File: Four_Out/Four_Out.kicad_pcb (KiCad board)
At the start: 2 copper layers, 60.7 x 66.3 mm, 23 parts, among them J1 String1, J2 String2, J3 String3, J4 String4, J5 Power In, J6 Expansion Header, U1 74LS125

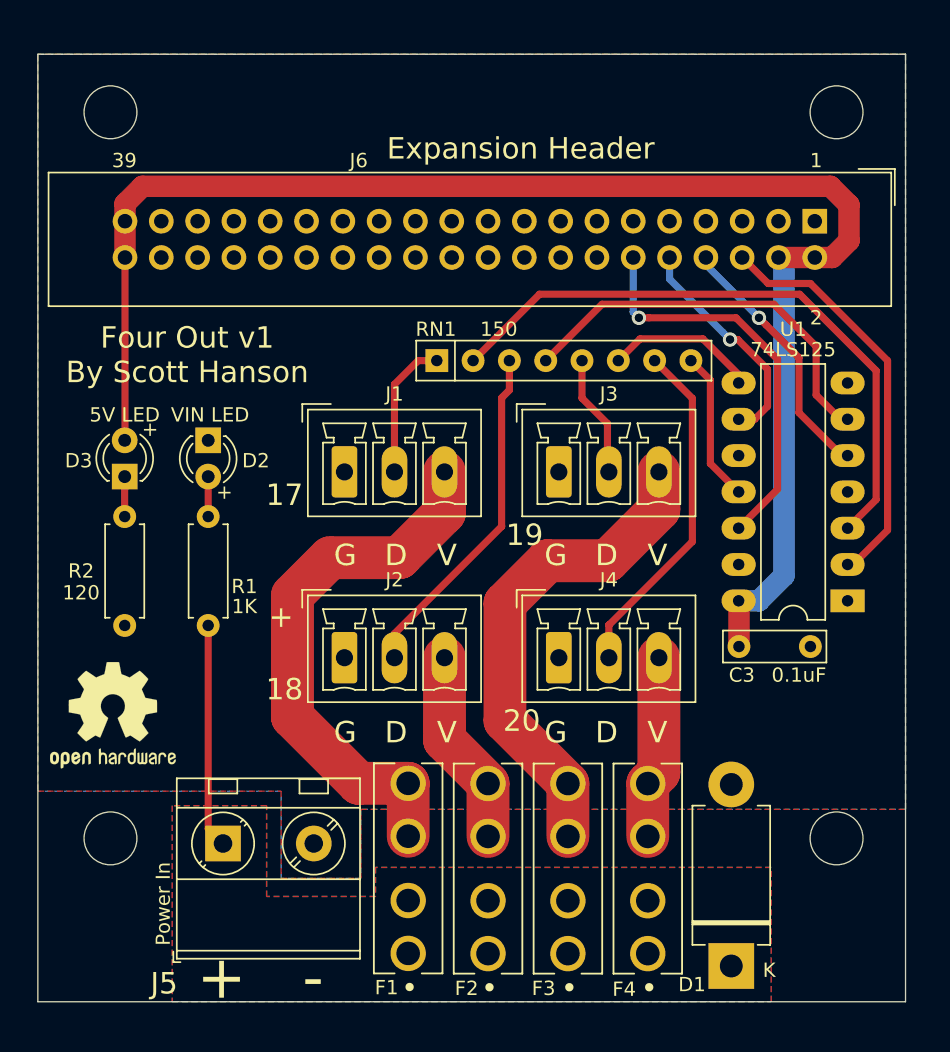
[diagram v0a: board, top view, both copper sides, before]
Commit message: fixed BOM, minor tweaks to ground plane and silkscreen
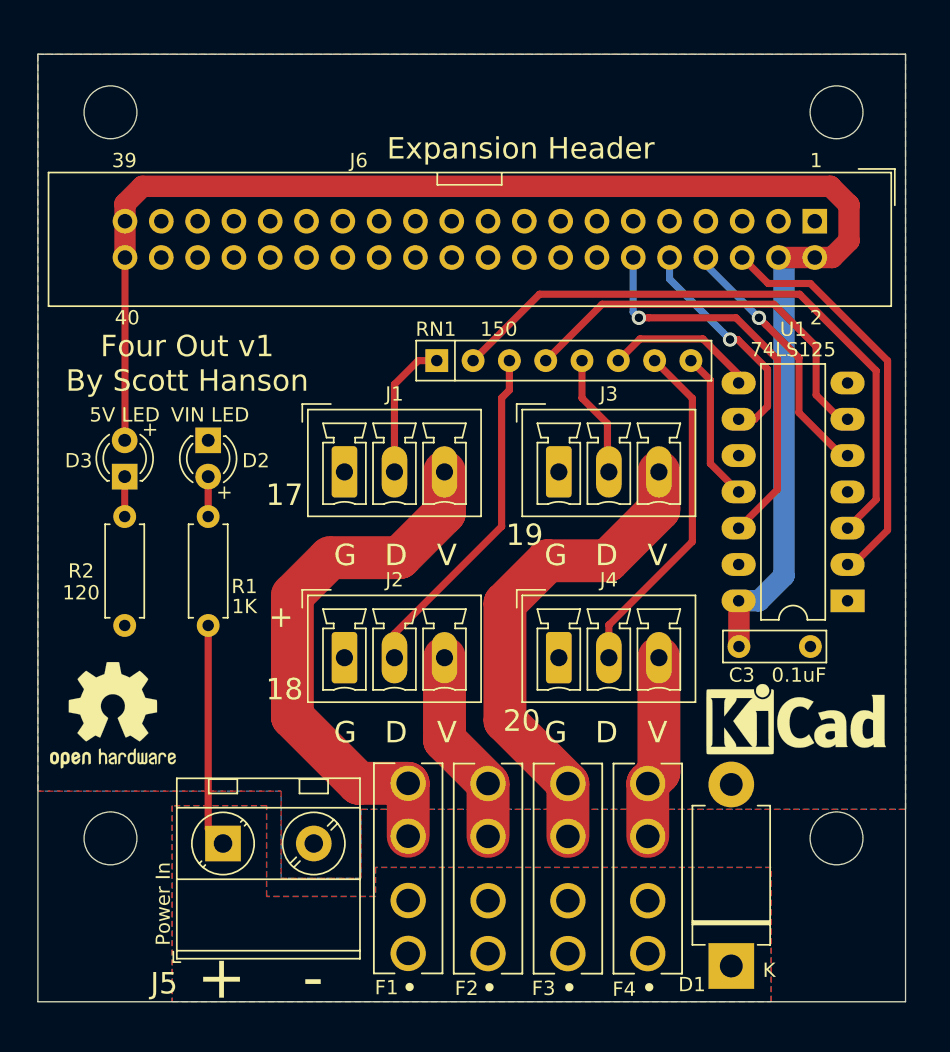
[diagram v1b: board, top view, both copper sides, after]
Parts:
- added REF**: KiCad-Logo_5mm_SilkScreen, Symbol:KiCad-Logo_5mm_SilkScreen, F.Cu at (120.7, 134.4)
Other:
- board text added: "40"

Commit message: rotated header and alt added screw header
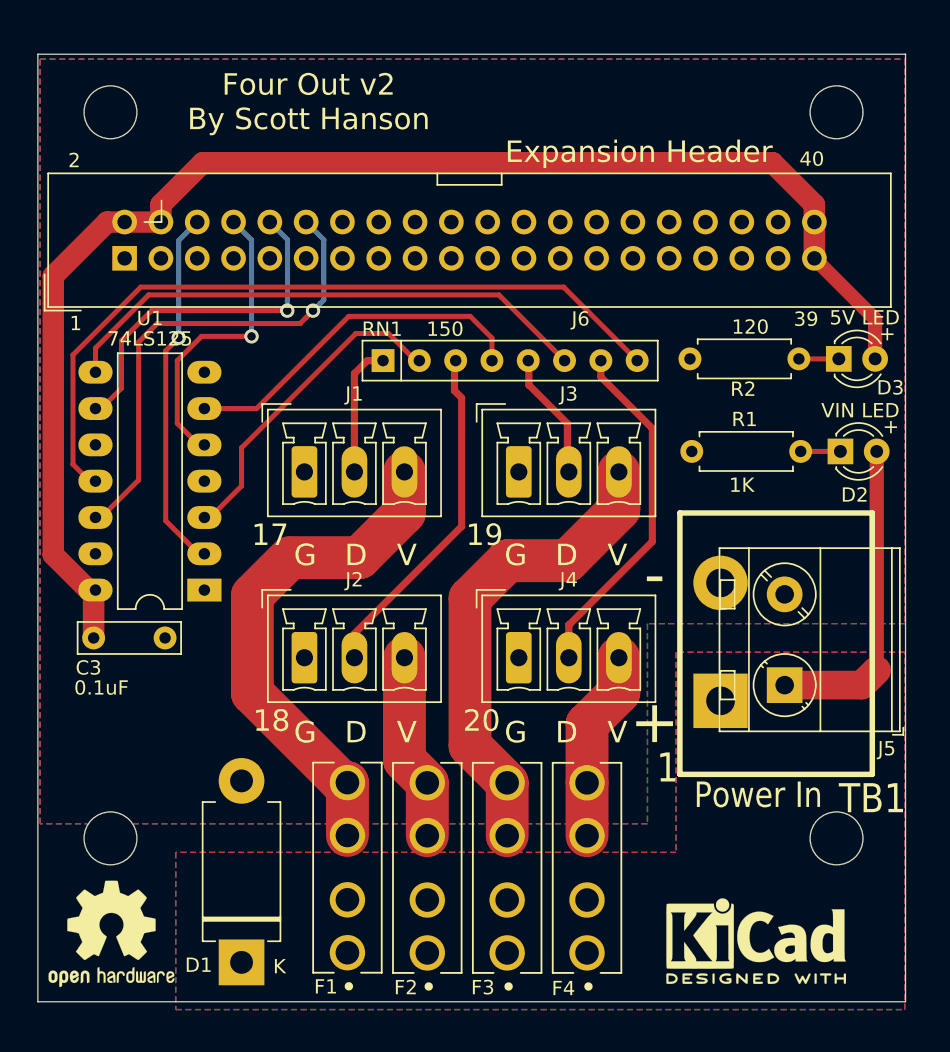
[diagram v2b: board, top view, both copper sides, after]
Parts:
- removed the REF** at (120.7, 134.4)
- added REF**: KiCad-Logo2_5mm_SilkScreen, Symbol:KiCad-Logo2_5mm_SilkScreen, F.Cu at (117.9, 149.4)
- added TB1: Power In, Barrier_Blocks:BARRIER_BLOCK_1ROW_2POS, F.Cu at (119.3, 128.6)
- moved D3 50.6 mm to (123.7, 108.7), turned to 0 degrees
- moved J6 48.4 mm to (73.7, 101.7), turned to 90 degrees
- moved C3 45.2 mm to (71.6, 128.2)
- moved U1 45.0 mm to (79.3, 124.9)
- moved D2 44.2 mm to (123.8, 115.2), turned to 0 degrees
- moved R2 43.7 mm to (113.3, 108.7), turned to 0 degrees
- moved J5 40.8 mm to (119.9, 131.5), turned to 90 degrees
- moved D1 34.3 mm to (81.9, 150.9)
- moved R1 34.1 mm to (113.4, 115.2), turned to 0 degrees
- moved REF** 15.3 mm to (72.8, 148.9)
- moved F1 4.25 mm to (89.3, 144.3)
- moved F2 4.25 mm to (94.9, 144.3)
- moved F3 4.25 mm to (100.5, 144.3)
- moved F4 4.25 mm to (106.1, 144.3)
- moved RN1 3.76 mm to (91.8, 108.8)
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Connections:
- D2 pad 1: GND -> Net-(D2-Pad1)
- D2 pad 2: Net-(D2-Pad2) -> VIN1
- R1 pad 1: Net-(D2-Pad2) -> GND
- R1 pad 2: VIN1 -> Net-(D2-Pad1)
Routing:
- net Net-(RN1-Pad8): track 10.6 -> 53.3 mm
- net Net-(RN1-Pad6): track 10.7 -> 38.0 mm
- net Net-(RN1-Pad2): track 44.2 -> 22.7 mm
- net OUT19: track 16.0 -> 24.9 mm
- net +5V: track 105.7 -> 97.9 mm
- net VIN1: track 15.7 -> 22.2 mm
- net OUT20: track 28.2 -> 33.9 mm
- net OUT17: track 28.8 -> 25.5 mm, vias 0 -> 1
- net OUT18: track 18.2 -> 21.3 mm
- net Net-(RN1-Pad4): track 28.1 -> 25.0 mm
- net Net-(D2-Pad2): track 2.79 -> 0.00 mm
- net Net-(D2-Pad1): track 0.00 -> 2.78 mm
- net /Output 1-8/VOUT1: track 38.1 -> 35.7 mm
- net /Output 1-8/VOUT3: track 34.2 -> 33.3 mm
- net /Output 1-8/VOUT2: track 13.8 -> 13.1 mm
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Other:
- net class Default: trace_width 0.5 -> 0.35
- board text added: "Four Out v2 By Scott Hanson"
- board text removed: "Four Out v1 By Scott Hanson"

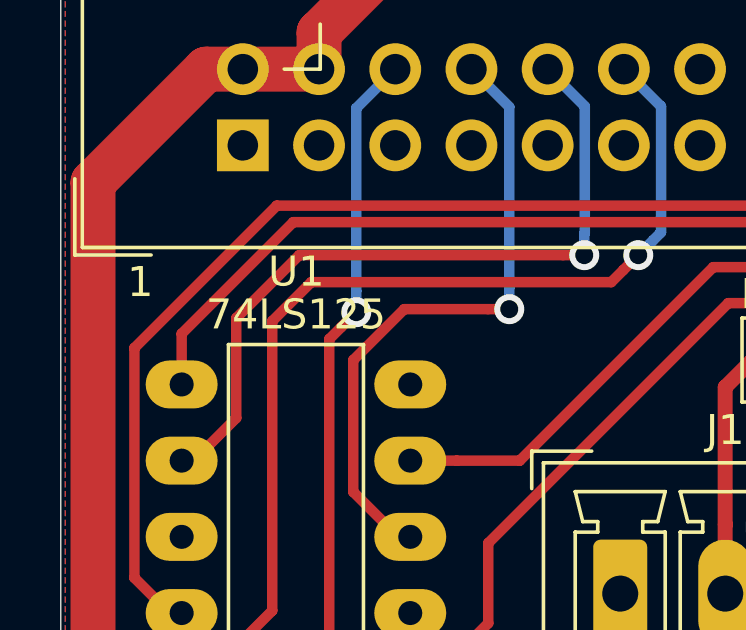
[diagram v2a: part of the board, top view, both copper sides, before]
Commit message: updated to 74HC125
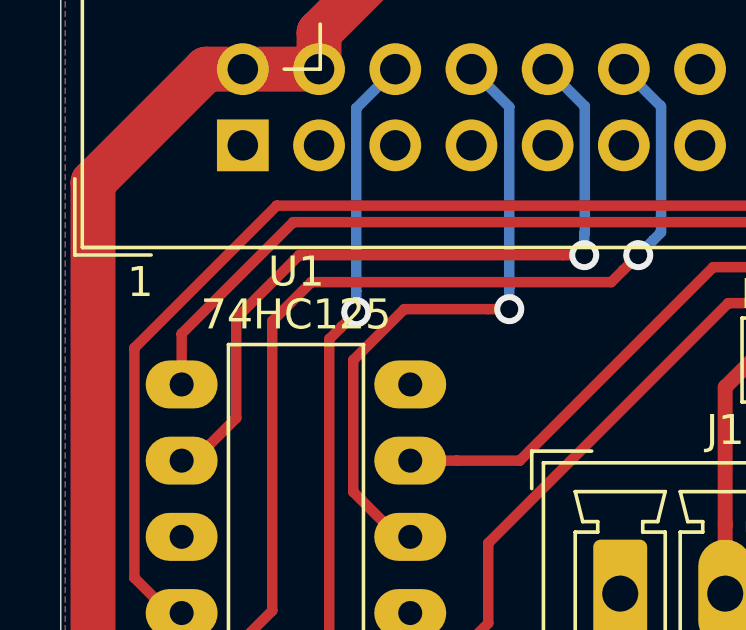
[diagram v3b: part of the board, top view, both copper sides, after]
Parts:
- U1: value 74LS125 -> 74HC125
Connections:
- net /Output 1-8/DOUT1 renamed /Output 1-4/DOUT1
- net /Output 1-8/DOUT2 renamed /Output 1-4/DOUT2
- net /Output 1-8/DOUT3 renamed /Output 1-4/DOUT3
- net /Output 1-8/DOUT4 renamed /Output 1-4/DOUT4
- net /Output 1-8/VOUT1 renamed /Output 1-4/VOUT1
- net /Output 1-8/VOUT2 renamed /Output 1-4/VOUT2
- net /Output 1-8/VOUT3 renamed /Output 1-4/VOUT3
- net /Output 1-8/VOUT4 renamed /Output 1-4/VOUT4

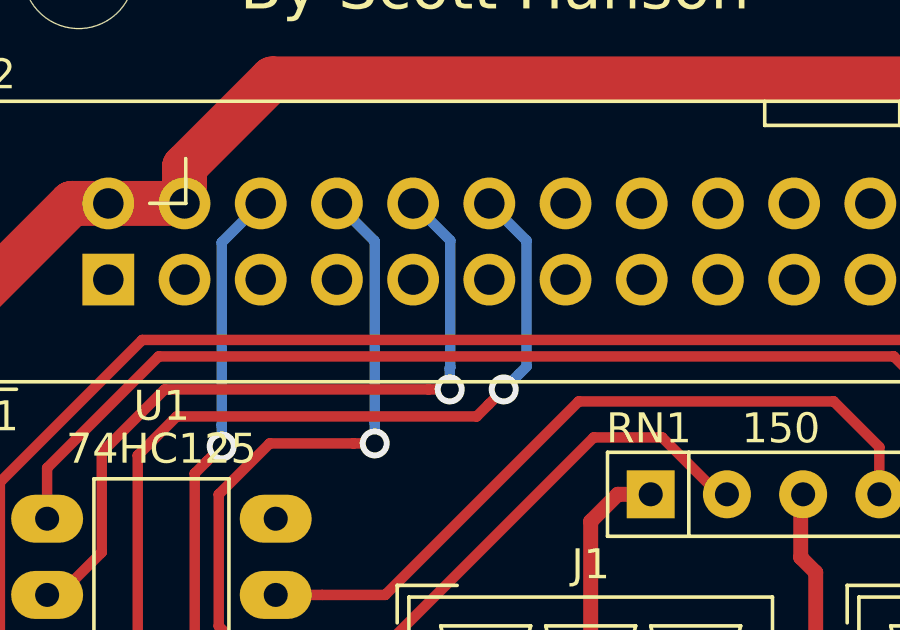
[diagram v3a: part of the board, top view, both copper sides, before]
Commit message: added Diff_Expansion
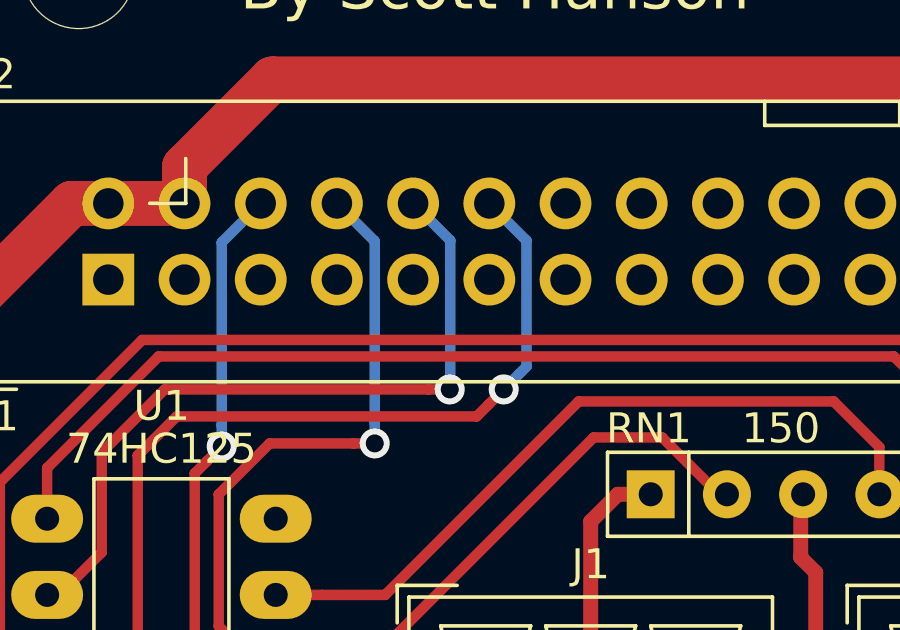
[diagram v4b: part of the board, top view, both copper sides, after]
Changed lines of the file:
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@@
     (thickness 1.6)
     (drawings 37)
-    (tracks 131)
+    (tracks 130)
     (zones 0)
     (modules 25)
@@
   (segment (start 74.701 117.1678) (end 74.701 107.5178) (width 0.35) (layer F.Cu) (net 8))
   (segment (start 86.001013 106.2178) (end 86.401014 105.817799) (width 0.35) (layer F.Cu) (net 8))
-  (segment (start 85.100984 104.610694) (end 85.100984 105.3178) (width 0.35) (layer B.Cu) (net 9))
   (segment (start 84.393878 105.3178) (end 85.100984 105.3178) (width 0.35) (layer F.Cu) (net 9))
-  (segment (start 85.119601 100.356401) (end 85.119601 104.592077) (width 0.35) (layer B.Cu) (net 9))
-  (segment (start 85.119601 104.592077) (end 85.100984 104.610694) (width 0.35) (layer B.Cu) (net 9))
   (segment (start 71.681 112.1678) (end 72.081 112.1678) (width 0.35) (layer F.Cu) (net 9))
   (segment (start 75.601 105.3178) (end 84.393878 105.3178) (width 0.35) (layer F.Cu) (net 9))
   (segment (start 73.501 107.4178) (end 75.601 105.3178) (width 0.35) (layer F.Cu) (net 9))
   (segment (start 73.501 110.7478) (end 73.501 107.4178) (width 0.35) (layer F.Cu) (net 9))
-  (segment (start 83.881 99.1178) (end 85.119601 100.356401) (width 0.35) (layer B.Cu) (net 9))
   (segment (start 72.081 112.1678) (end 73.501 110.7478) (width 0.35) (layer F.Cu) (net 9))
   (via (at 85.100984 105.3178) (size 1) (drill 0.6) (layers F.Cu B.Cu) (net 9))
+  (segment (start 85.119601 105.299183) (end 85.100984 105.3178) (width 0.35) (layer B.Cu) (net 9))
+  (segment (start 83.881 99.1178) (end 85.119601 100.356401) (width 0.35) (layer B.Cu) (net 9))
+  (segment (start 85.119601 100.356401) (end 85.119601 105.299183) (width 0.35) (layer B.Cu) (net 9))
   (segment (start 82.601 100.3778) (end 82.601 106.410686) (width 0.35) (layer B.Cu) (net 10))
   (segment (start 82.601 106.410686) (end 82.601 107.117792) (width 0.35) (layer B.Cu) (net 10))

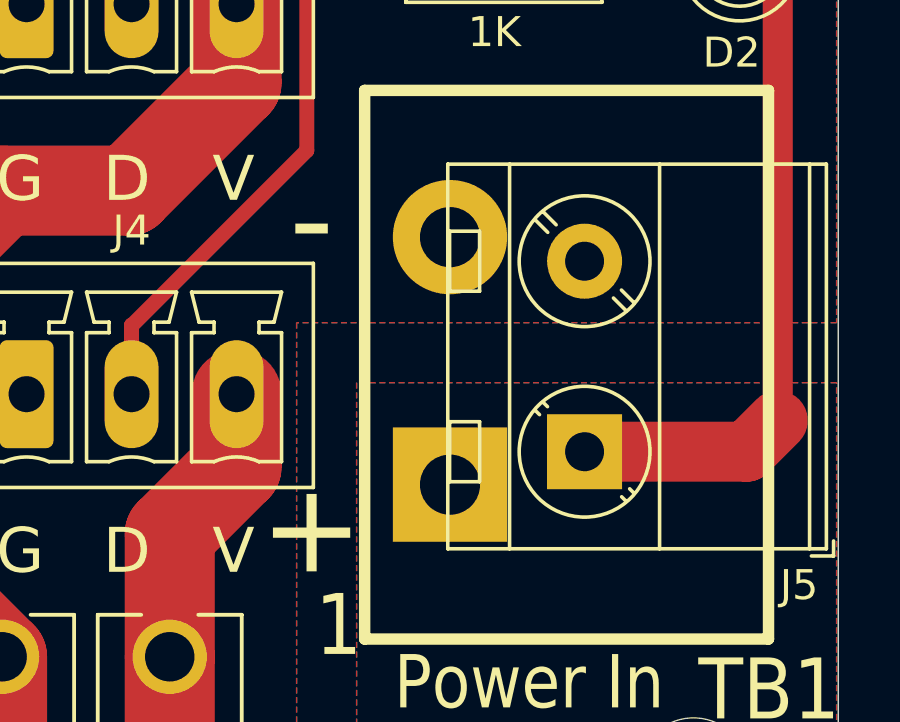
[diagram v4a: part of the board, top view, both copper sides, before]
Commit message: adjusted holes sizes for screw terminals
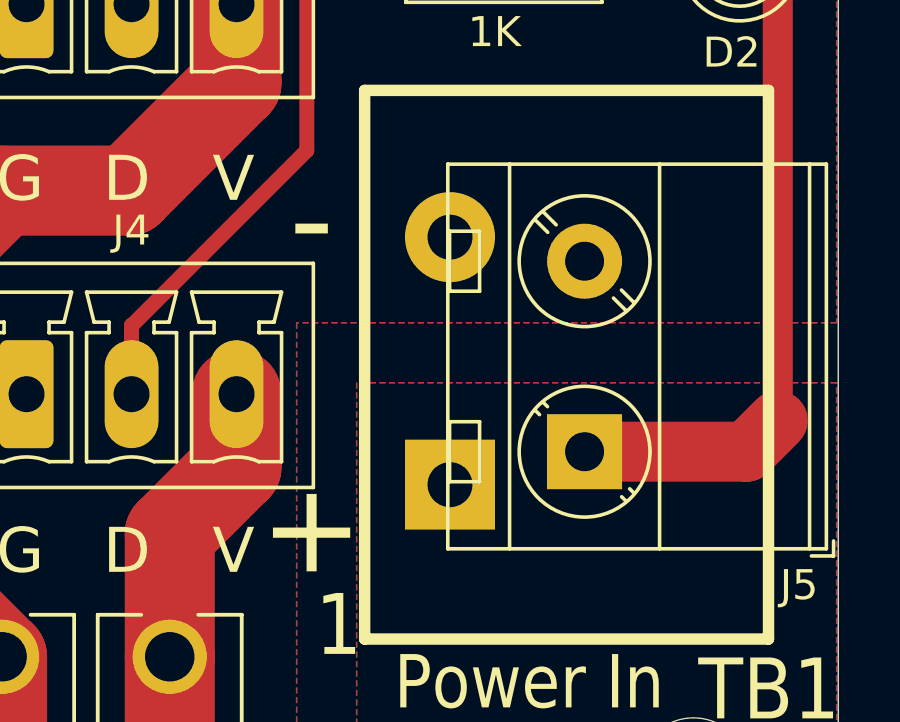
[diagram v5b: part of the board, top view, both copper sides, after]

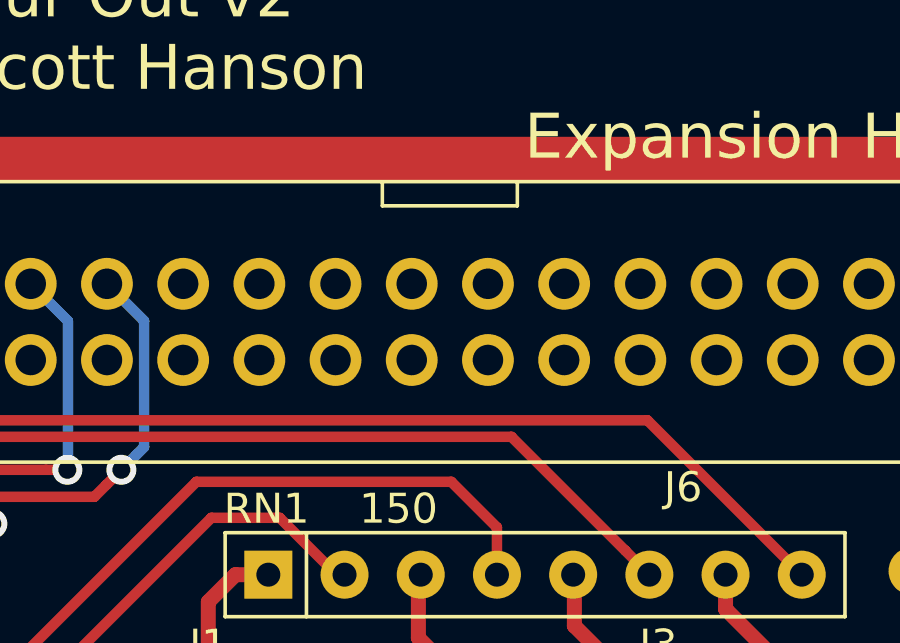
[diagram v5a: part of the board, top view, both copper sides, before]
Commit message: fix header silkscreen
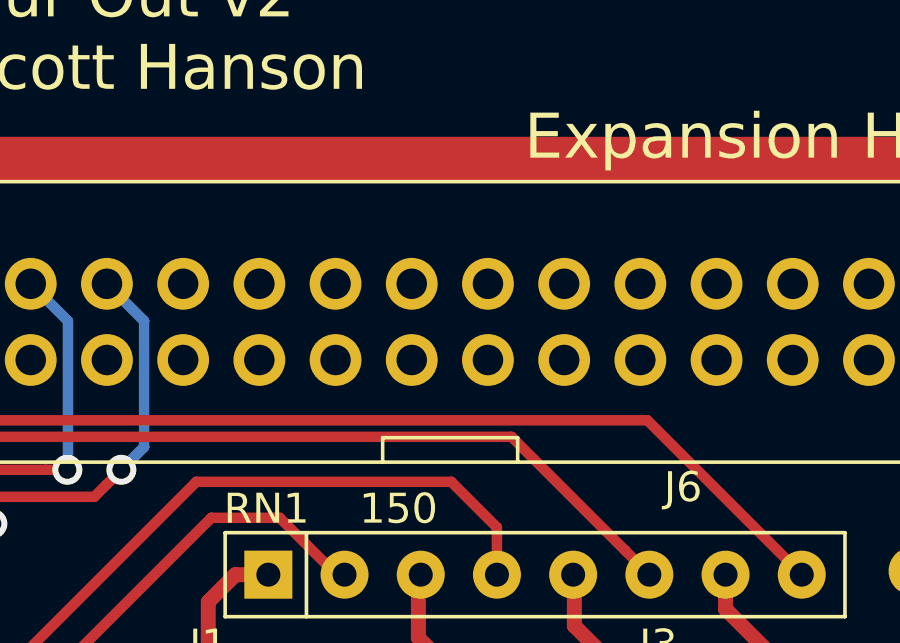
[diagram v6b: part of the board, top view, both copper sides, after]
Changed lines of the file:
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@@
-(kicad_pcb (version 20171130) (host pcbnew "(5.1.5)-3")
+(kicad_pcb (version 20171130) (host pcbnew "(5.1.2)-1")
   (general
     (thickness 1.6)
@@
     (effects (font (size 1 1) (thickness 0.15)))
   )
-  (gr_line (start 100.101 96.5178) (end 100.101 95.7178) (layer F.SilkS) (width 0.12))
-  (gr_line (start 95.601 96.5178) (end 100.101 96.5178) (layer F.SilkS) (width 0.12))
-  (gr_line (start 95.601 95.7178) (end 95.601 96.5178) (layer F.SilkS) (width 0.12))
+  (gr_line (start 95.611 104.2478) (end 95.611 105.0478) (layer F.SilkS) (width 0.12))
+  (gr_line (start 100.111 104.2478) (end 95.611 104.2478) (layer F.SilkS) (width 0.12))
+  (gr_line (start 100.111 105.0478) (end 100.111 104.2478) (layer F.SilkS) (width 0.12))
   (gr_text 39 (at 121.401 105.9178) (layer F.SilkS)
     (effects (font (size 1 1) (thickness 0.15)))
